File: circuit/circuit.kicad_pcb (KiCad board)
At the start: 2 copper layers, 30.5 x 42.2 mm, 10 parts, among them SW1 SW_Push, U1 ATtiny10-TS

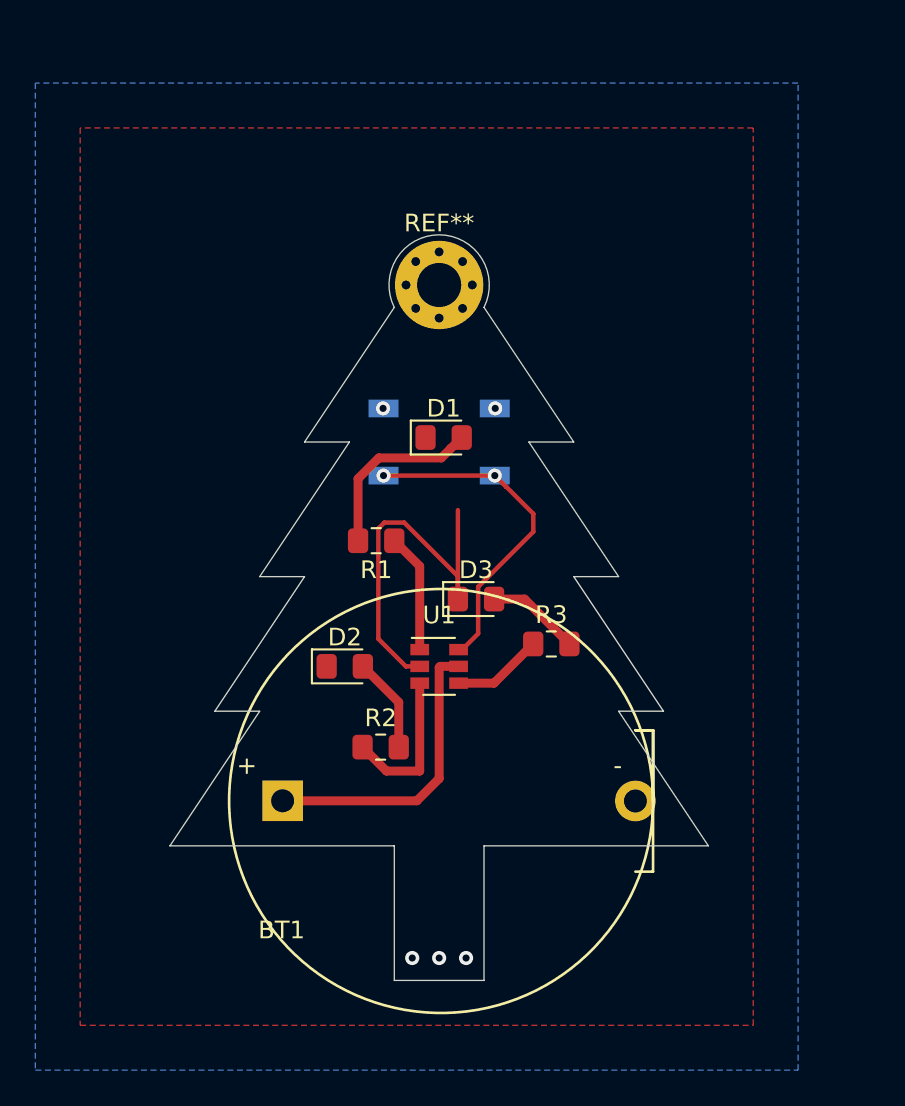
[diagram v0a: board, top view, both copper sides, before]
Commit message: Update schematic info and use the good version
Update schematic info and use the good version of the files, delete old Gerbers
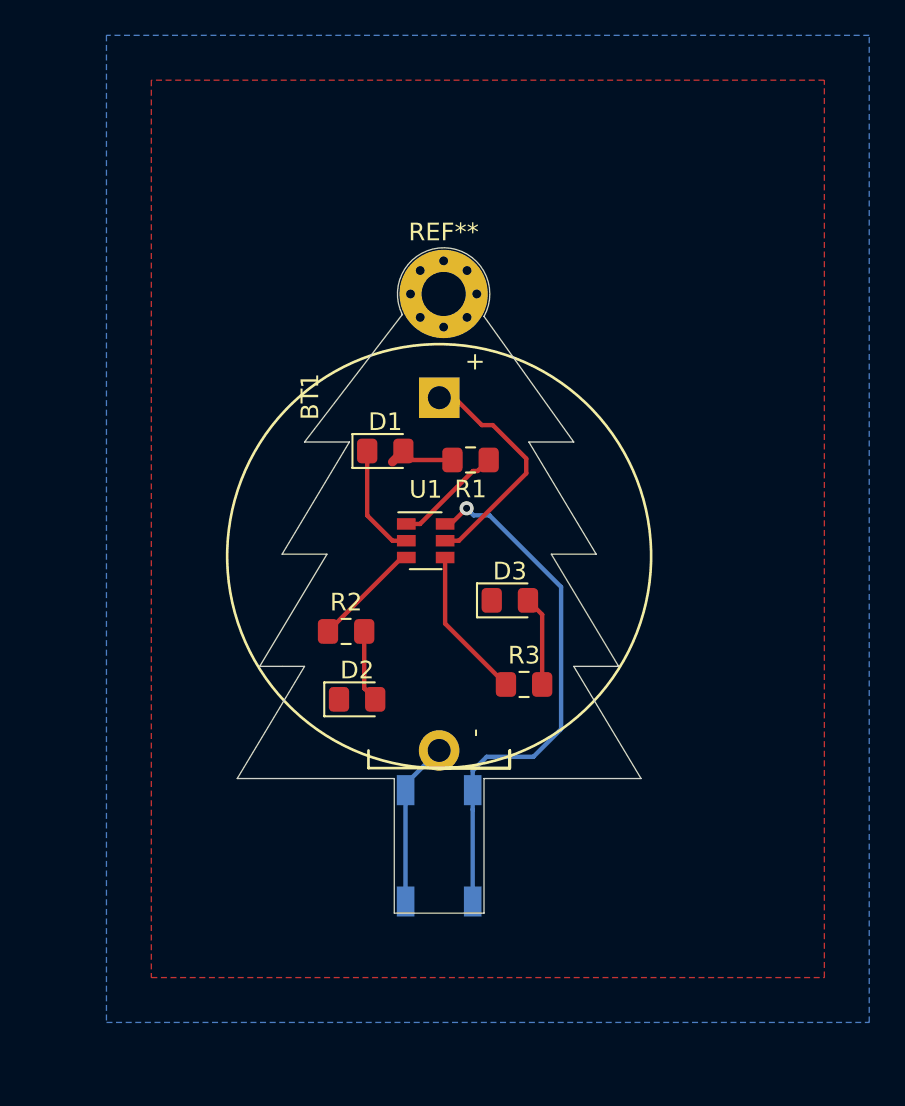
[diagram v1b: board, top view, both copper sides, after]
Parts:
- moved BT1 24.5 mm to (63.5, 50.8), turned to 270 degrees
- moved SW1 22.9 mm to (63.5, 76.2), turned to 90 degrees
- moved U1 7.15 mm to (62.7, 58.9)
- moved R1 7.03 mm to (65.3, 54.4)
- moved R2 6.84 mm to (58.2, 64.1)
- moved D1 3.39 mm to (60.5, 53.8)
- moved R3 2.76 mm to (68.3, 67.1)
- moved D2 1.99 mm to (58.9, 67.9)
- moved D3 1.92 mm to (67.5, 62.3)
- moved REF** 0.57 mm to (63.8, 45.0)
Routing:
- net Net-(SW1-Pad1): track 18.9 -> 30.2 mm, vias 2 -> 1
- net Net-(D1-Pad2): track 10.3 -> 3.87 mm
- net Net-(BT1-Pad2): track 21.5 -> 15.8 mm, vias 5 -> 0
- net Net-(R3-Pad1): track 5.14 -> 8.61 mm
- net Net-(BT1-Pad1): track 16.8 -> 13.4 mm
- net Net-(R2-Pad1): track 8.98 -> 6.16 mm
- net Net-(D2-Pad2): track 5.41 -> 4.10 mm
- net Net-(R1-Pad1): track 6.76 -> 6.17 mm
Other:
- board size 30.5 x 42.2 mm -> 22.9 x 37.7 mm

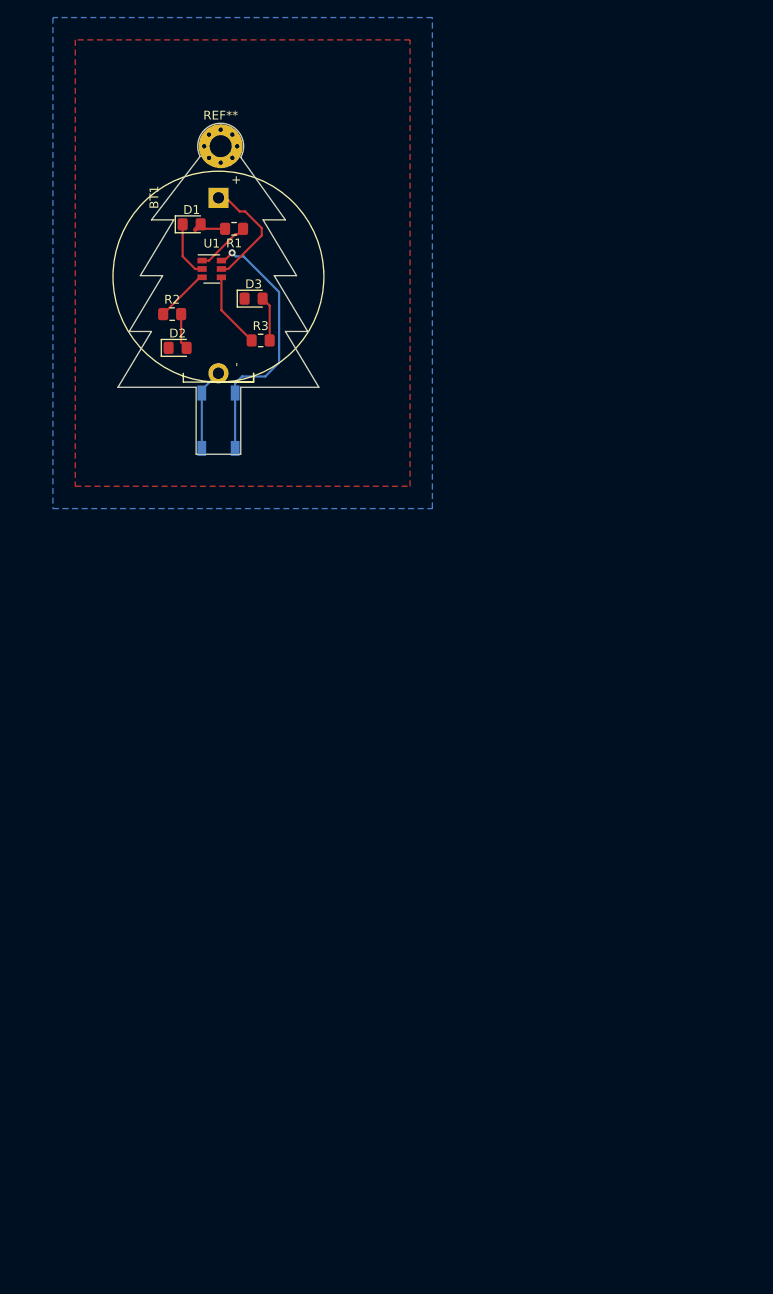
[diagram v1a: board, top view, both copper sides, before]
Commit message: Correct battery polarity
Correct battery polarity, update PCB info
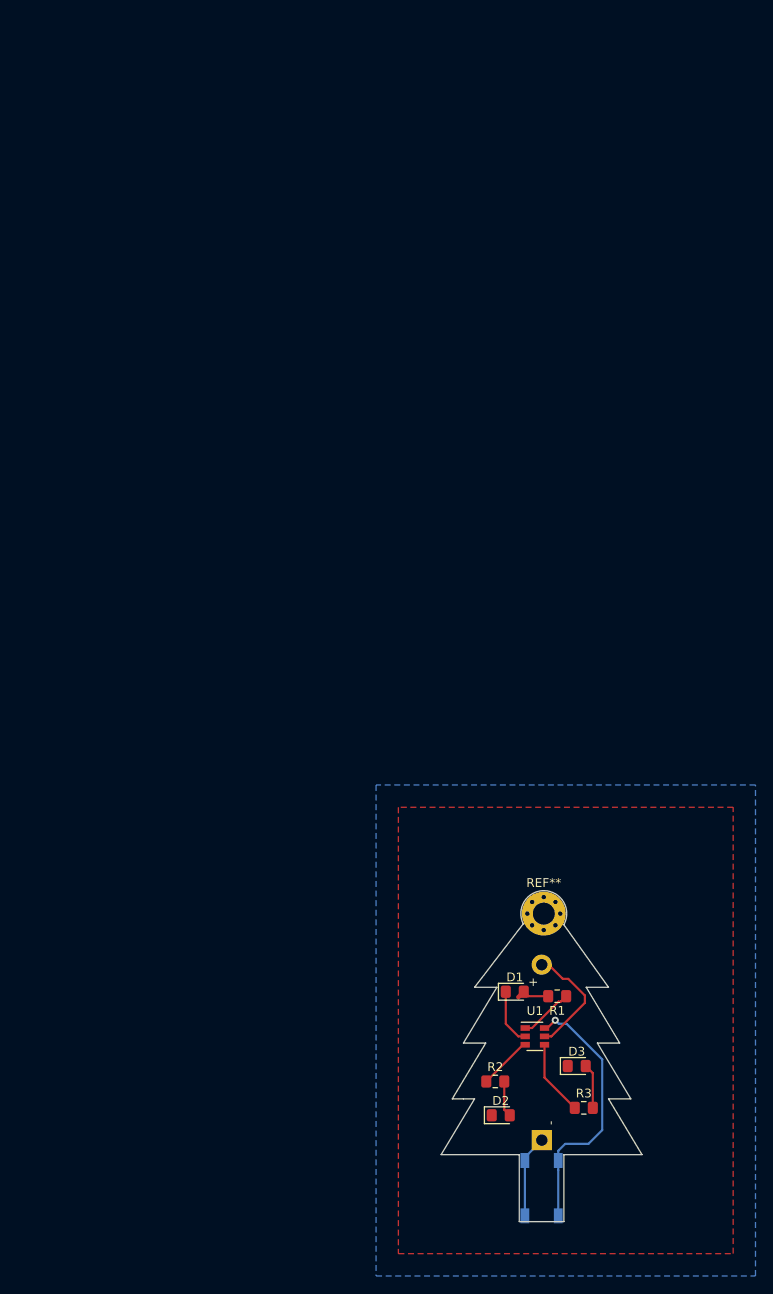
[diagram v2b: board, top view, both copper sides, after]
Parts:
- BT1: moved to B.Cu
- moved BT1 113.4 mm to (100.3, 158.1), turned to 90 degrees
- moved REF** 94.8 mm to (100.5, 132.3)
- moved D1 94.8 mm to (97.2, 141.2)
- moved D2 94.8 mm to (95.6, 155.2)
- moved R3 94.8 mm to (105.1, 154.4)
- moved SW1 94.8 mm to (100.3, 163.5)
- moved D3 94.8 mm to (104.3, 149.6)
- moved R1 94.8 mm to (102.0, 141.7)
- moved R2 94.8 mm to (95.0, 151.4)
- moved U1 94.8 mm to (99.5, 146.3)
